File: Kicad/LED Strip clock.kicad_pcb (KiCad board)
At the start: 2 copper layers, 99.1 x 97.8 mm, 81 parts, among them J1 Conn_01x09_Male, J2 Conn_01x09_Male, J3 Conn_01x09_Male, J4 Conn_01x09_Male, J5 Conn_01x04_Male, J6 Barrel_Jack_Switch, U1 TPIC6B595, U10 5611BH, U11 5611BH, U12 5611BH, U13 MCP23008-xSO, U14 INA219AxDCN, U2 TPIC6B595, U3 TPIC6B595, U4 TPIC6B595, U5 74HCT244, U6 WeMos_D1_mini, U7 MAX809S, U8 L7805, U9 5611BH

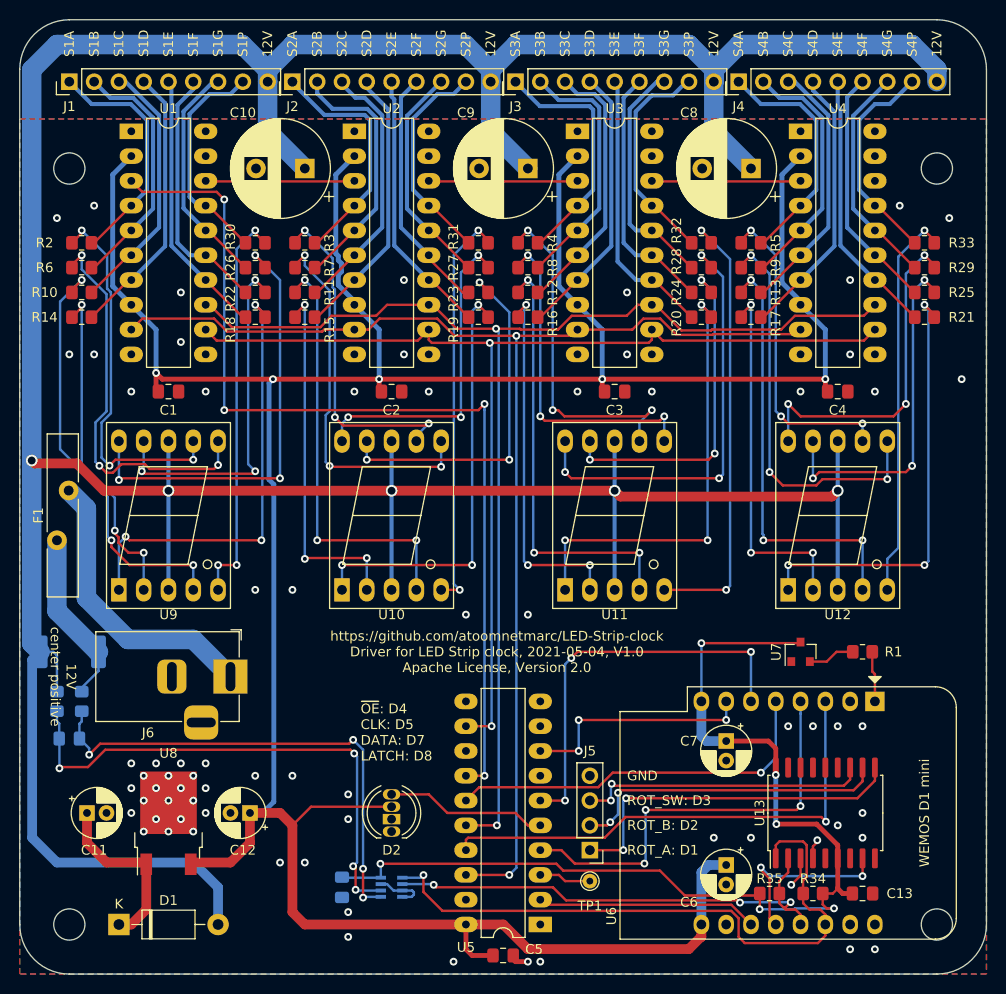
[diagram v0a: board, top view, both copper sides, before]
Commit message: Changed INA219AxDCN to INA219AxD.
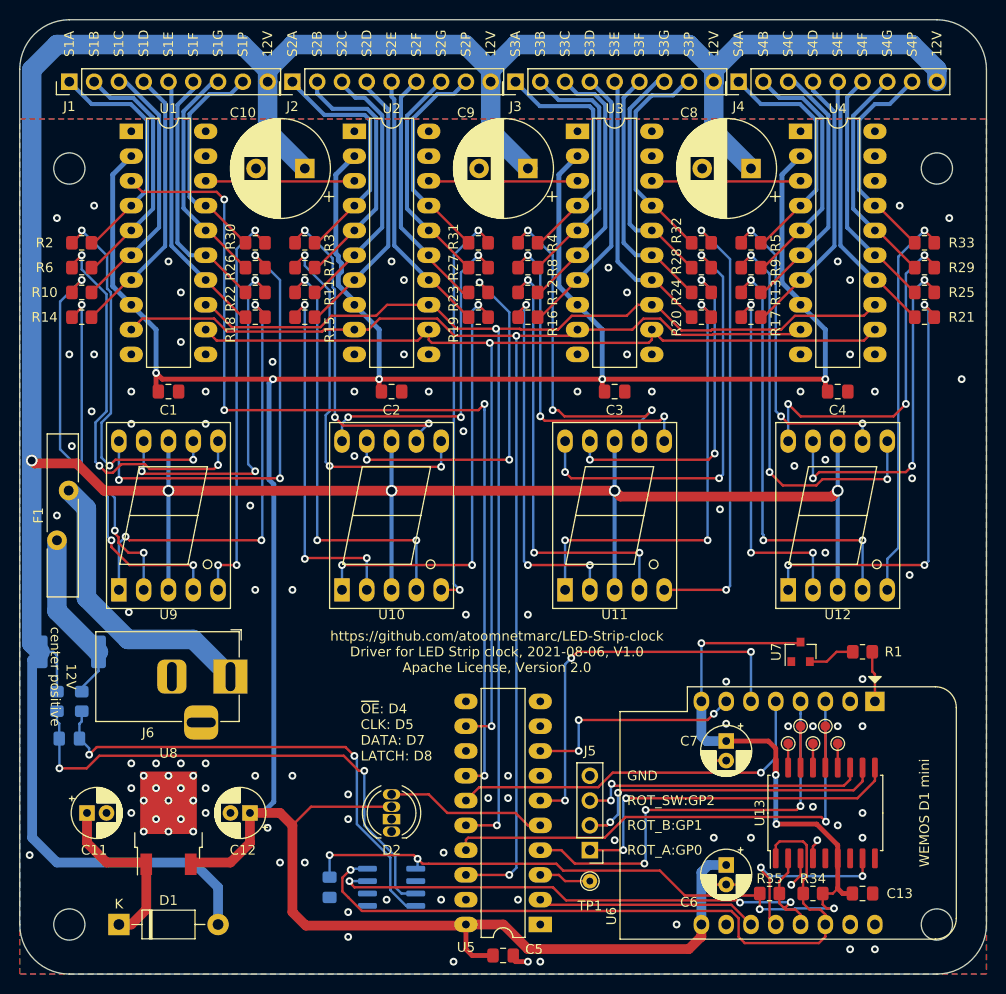
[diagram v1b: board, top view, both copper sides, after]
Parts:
- added TP2: TestPoint, TestPoint:TestPoint_Pad_D1.0mm, F.Cu at (226.1, 132.6)
- added TP3: TestPoint, TestPoint:TestPoint_Pad_D1.0mm, F.Cu at (224.8, 130.8)
- added TP4: TestPoint, TestPoint:TestPoint_Pad_D1.0mm, F.Cu at (223.5, 132.6)
- added TP5: TestPoint, TestPoint:TestPoint_Pad_D1.0mm, F.Cu at (222.2, 130.8)
- added TP6: TestPoint, TestPoint:TestPoint_Pad_D1.0mm, F.Cu at (221.0, 132.6)
- U14: value INA219AxDCN -> INA219AxD; footprint Package_TO_SOT_SMD:SOT-23-8 -> Package_SO:SOIC-8_3.9x4.9mm_P1.27mm
- moved C14 1.27 mm to (174.0, 147.3)
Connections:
- U14 pad 1: Net-(C15-Pad1) -> GND
- U14 pad 2: Net-(C15-Pad2) -> GND
- U14 pad 3: GND -> SDA
- U14 pad 4: +3V3 -> SCL
- U14 pad 5: SCL -> +3V3
- U14 pad 6: SDA -> GND
- U14 pad 7: GND -> Net-(C15-Pad2)
- U14 pad 8: GND -> Net-(C15-Pad1)
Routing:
- net SCL: track 64.7 -> 73.4 mm
- net SDA: track 50.2 -> 57.6 mm
- net Net-(TP5-Pad1): track 0.00 -> 4.24 mm
- net Net-(TP3-Pad1): track 0.00 -> 4.24 mm
- net +3V3: track 108.3 -> 111.7 mm, vias 6 -> 7
- net Net-(TP6-Pad1): track 0.00 -> 2.46 mm
- net Net-(TP4-Pad1): track 0.00 -> 2.46 mm
- net Net-(TP2-Pad1): track 0.00 -> 2.46 mm
- net /LATCH: track 24.1 -> 23.0 mm
- net GND: track 12.4 -> 12.9 mm, vias 72 -> 107
- net Net-(C15-Pad1): track 51.1 -> 51.4 mm, vias 4 -> 2
- net Net-(C15-Pad2): track 54.1 -> 54.0 mm, vias 4 -> 2
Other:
- board text added: "ROT_A:GP0"
- board text added: "ROT_B:GP1"
- board text added: "ROT_SW:GP2"
- board text added: "https://github.com/atoomnetmarc/LED-Strip-clock Driver for LED Strip clock, 2021-08-06, V1.0 Apache License, Version 2.0"
- board text removed: "ROT_A: D1"
- board text removed: "ROT_B: D2"
- board text removed: "ROT_SW: D3"
- board text removed: "https://github.com/atoomnetmarc/LED-Strip-clock Driver for LED Strip clock, 2021-05-04, V1.0 Apache License, Version 2.0"
